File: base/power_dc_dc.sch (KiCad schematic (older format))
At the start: 14 parts

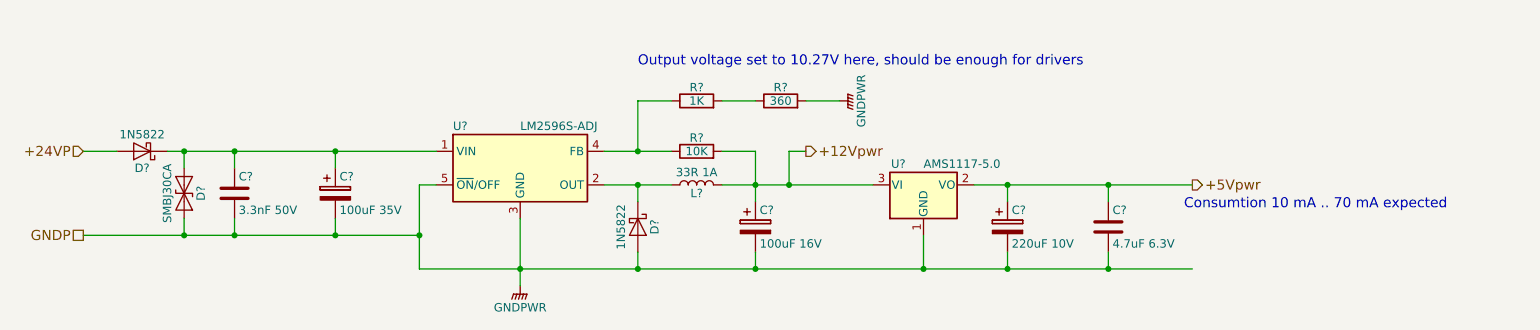
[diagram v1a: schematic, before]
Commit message: Update base board: 1. Add extra analog voltage input to core board.   -> update pinmux 2. Assign most footprints. 3. Generate netlist. 4. Add core_sf board. 5. Add kicad_symbols library submodule.
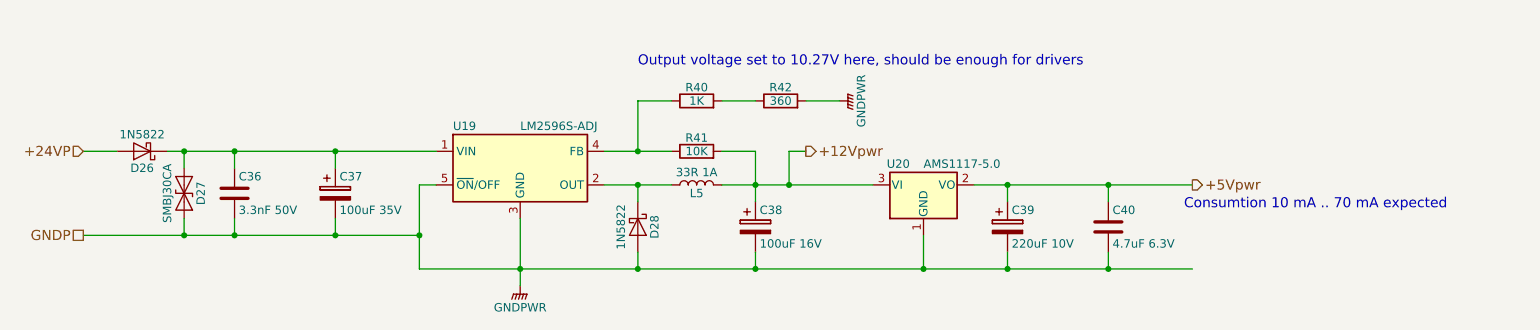
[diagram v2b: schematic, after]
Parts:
- U19: renamed from U?; footprint TO_SOT_Packages_SMD:TO-263-5_TabPin3 -> Package_TO_SOT_SMD:TO-263-5_TabPin3
- gave numbers to parts that had none: 13
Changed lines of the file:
@@
 GNDP
 $Comp
-L CP C?
+L CP C37
 U 1 1 5A3CC87A
 P 4400 1950
-F 0 "C?" H 4425 2050 50  0000 L CNN
+F 0 "C37" H 4425 2050 50  0000 L CNN
 F 1 "100uF 35V" H 4425 1850 50  0000 L CNN
 F 2 "Capacitor_SMD:CP_Elec_6.3x7.7" H 4438 1800 50  0001 C CNN
@@
 $EndComp
 $Comp
-L 1N5822 D?
+L 1N5822 D26
 U 1 1 5A3CCF01
 P 3250 1700
-F 0 "D?" H 3250 1800 50  0000 C CNN
+F 0 "D26" H 3250 1800 50  0000 C CNN
 F 1 "1N5822" H 3250 1600 50  0000 C CNN
 F 2 "Diode_SMD:D_SMA" H 3250 1525 50  0001 C CNN
@@
 $EndComp
 $Comp
-L D_TVS D?
+L D_TVS D27
 U 1 1 5A3CCF8D
 P 3500 1950
-F 0 "D?" H 3500 2050 50  0000 C CNN
+F 0 "D27" H 3500 2050 50  0000 C CNN
 F 1 "SMBJ30CA" H 3500 1850 50  0000 C CNN
 F 2 "Diode_SMD:D_SMB" H 3500 1950 50  0001 C CNN
@@
 $EndComp
 $Comp
-L C C?
+L C C36
 U 1 1 5A3CD01A
 P 3800 1950
-F 0 "C?" H 3825 2050 50  0000 L CNN
+F 0 "C36" H 3825 2050 50  0000 L CNN
 F 1 "3.3nF 50V" H 3825 1850 50  0000 L CNN
 F 2 "Capacitor_SMD:C_0603_1608Metric" H 3838 1800 50  0001 C CNN
@@
 Connection ~ 4400 1700
 $Comp
-L CP C?
+L CP C38
 U 1 1 5A3CE026
 P 6900 2150
-F 0 "C?" H 6925 2250 50  0000 L CNN
+F 0 "C38" H 6925 2250 50  0000 L CNN
 F 1 "100uF 16V" H 6925 2050 50  0000 L CNN
 F 2 "Capacitor_SMD:CP_Elec_6.3x5.3" H 6938 2000 50  0001 C CNN
@@
 $EndComp
 $Comp
-L AP1117-15 U?
+L AP1117-15 U20
 U 1 1 5A3CE6FE
 P 7900 1900
-F 0 "U?" H 7750 2025 50  0000 C CNN
+F 0 "U20" H 7750 2025 50  0000 C CNN
 F 1 "AMS1117-5.0" H 7900 2025 50  0000 L CNN
 F 2 "Package_TO_SOT_SMD:SOT-223" H 7900 2100 50  0001 C CNN
@@
 	7900 2400 7900 2200
 $Comp
-L CP C?
+L CP C39
 U 1 1 5A3CEB23
 P 8400 2150
-F 0 "C?" H 8425 2250 50  0000 L CNN
+F 0 "C39" H 8425 2250 50  0000 L CNN
 F 1 "220uF 10V" H 8425 2050 50  0000 L CNN
 F 2 "Capacitor_SMD:CP_Elec_6.3x5.3" H 8438 2000 50  0001 C CNN
@@
 	8400 1900 8400 2000
 $Comp
-L C C?
+L C C40
 U 1 1 5A3CEF52
 P 9000 2150
-F 0 "C?" H 9025 2250 50  0000 L CNN
+F 0 "C40" H 9025 2250 50  0000 L CNN
 F 1 "4.7uF 6.3V" H 9025 2050 50  0000 L CNN
 F 2 "Capacitor_SMD:C_0603_1608Metric" H 9038 2000 50  0001 C CNN
@@
 	2900 2200 4900 2200
 $Comp
-L LM2596S-ADJ U?
+L LM2596S-ADJ U19
 U 1 1 5A3D049F
 P 5500 1800
-F 0 "U?" H 5100 2050 50  0000 L CNN
+F 0 "U19" H 5100 2050 50  0000 L CNN
 F 1 "LM2596S-ADJ" H 5500 2050 50  0000 L CNN
-F 2 "TO_SOT_Packages_SMD:TO-263-5_TabPin3" H 5550 1550 50  0001 L CIN
+F 2 "Package_TO_SOT_SMD:TO-263-5_TabPin3" H 5550 1550 50  0001 L CIN
 F 3 "" H 5500 1800 50  0001 C CNN
 	1    5500 1800
@@
 $EndComp
 $Comp
-L 1N5822 D?
+L 1N5822 D28
 U 1 1 5A3D0B74
 P 6200 2150
-F 0 "D?" H 6200 2250 50  0000 C CNN
+F 0 "D28" H 6200 2250 50  0000 C CNN
 F 1 "1N5822" H 6200 2050 50  0000 C CNN
 F 2 "Diode_SMD:D_SMA" H 6200 1975 50  0001 C CNN
@@
 	6000 1900 6400 1900
 $Comp
-L L L?
+L L L5
 U 1 1 5A3D14CE
 P 6550 1900
-F 0 "L?" V 6500 1900 50  0000 C CNN
+F 0 "L5" V 6500 1900 50  0000 C CNN
 F 1 "33R 1A" V 6625 1900 50  0000 C CNN
 F 2 "Inductor_SMD:L_7.3x7.3_H3.5" H 6550 1900 50  0001 C CNN
@@
 	6000 1700 6400 1700
 $Comp
-L R R?
+L R R41
 U 1 1 5A3D2233
 P 6550 1700
-F 0 "R?" V 6630 1700 50  0000 C CNN
+F 0 "R41" V 6630 1700 50  0000 C CNN
 F 1 "10K" V 6550 1700 50  0000 C CNN
 F 2 "Resistor_SMD:R_0603_1608Metric" V 6480 1700 50  0001 C CNN
@@
 $EndComp
 $Comp
-L R R?
+L R R40
 U 1 1 5A3D2341
 P 6550 1400
-F 0 "R?" V 6630 1400 50  0000 C CNN
+F 0 "R40" V 6630 1400 50  0000 C CNN
 F 1 "1K" V 6550 1400 50  0000 C CNN
 F 2 "Resistor_SMD:R_0603_1608Metric" V 6480 1400 50  0001 C CNN
@@
 	6700 1400 6900 1400
 $Comp
-L R R?
+L R R42
 U 1 1 5A3D26F4
 P 7050 1400
-F 0 "R?" V 7130 1400 50  0000 C CNN
+F 0 "R42" V 7130 1400 50  0000 C CNN
 F 1 "360" V 7050 1400 50  0000 C CNN
 F 2 "Resistor_SMD:R_0603_1608Metric" V 6980 1400 50  0001 C CNN
@@
 	7200 1400 7400 1400
 $Comp
-L GNDPWR #PWR?
+L GNDPWR #PWR025
 U 1 1 5A3D27D8
 P 7400 1400
-F 0 "#PWR?" H 7400 1200 50  0001 C CNN
+F 0 "#PWR025" H 7400 1200 50  0001 C CNN
 F 1 "GNDPWR" H 7400 1270 50  0000 C CNN
 F 2 "" H 7400 1350 50  0001 C CNN
@@
 $EndComp
 $Comp
-L GNDPWR #PWR?
+L GNDPWR #PWR026
 U 1 1 5A3D2843
 P 5500 2500
-F 0 "#PWR?" H 5500 2300 50  0001 C CNN
+F 0 "#PWR026" H 5500 2300 50  0001 C CNN
 F 1 "GNDPWR" H 5500 2370 50  0000 C CNN
 F 2 "" H 5500 2450 50  0001 C CNN

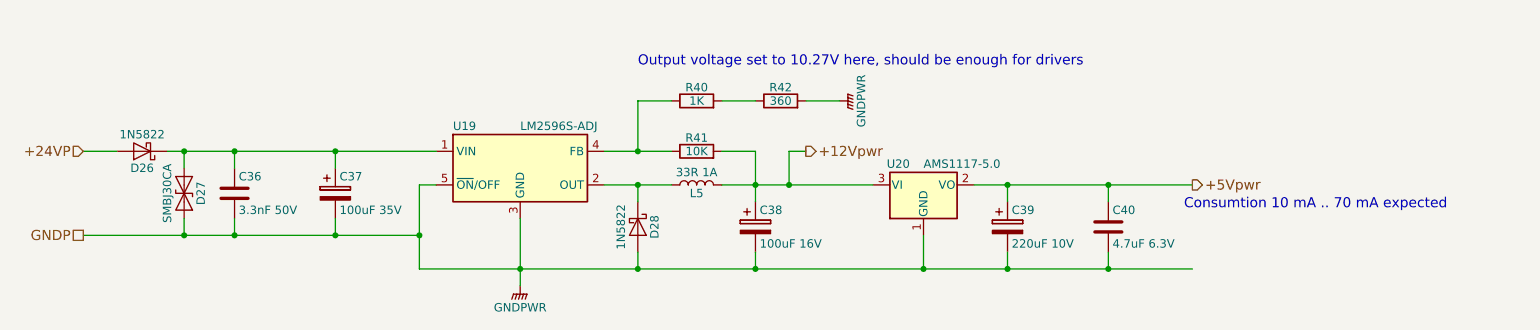
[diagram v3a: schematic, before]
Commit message: some test points
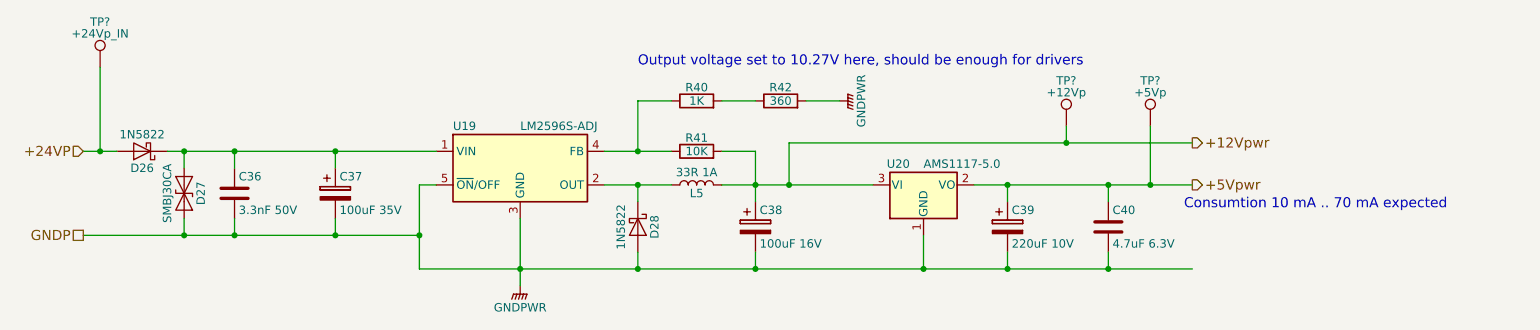
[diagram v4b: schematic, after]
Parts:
- added TP?: +24Vp_IN, symbol Test_Point
- added TP?: +12Vp, symbol Test_Point
- added TP?: +5Vp, symbol Test_Point
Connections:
- net +12Vpwr: now also TP?.1
- net +24VP: now also TP?.1
- net +5Vpwr: now also TP?.1
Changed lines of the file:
@@
 Text HLabel 2900 1700 0    60   Input ~ 0
 +24VP
-Text HLabel 7200 1700 2    60   Output ~ 0
+Text HLabel 9500 1650 2    60   Output ~ 0
 +12Vpwr
 Text HLabel 9500 1900 2    60   Output ~ 0
@@
 	1    0    0    -1
 $EndComp
-Wire Wire Line
-	3400 1700 5000 1700
-Wire Wire Line
-	2900 1700 3100 1700
-Wire Wire Line
-	3500 1800 3500 1700
-Connection ~ 3500 1700
-Wire Wire Line
-	4400 2100 4400 2200
-Connection ~ 4400 2200
-Wire Wire Line
-	3800 2100 3800 2200
-Connection ~ 3800 2200
-Wire Wire Line
-	3500 2100 3500 2200
-Connection ~ 3500 2200
-Wire Wire Line
-	3800 1800 3800 1700
-Connection ~ 3800 1700
-Wire Wire Line
-	4400 1800 4400 1700
-Connection ~ 4400 1700
 $Comp
 L CP C38
@@
 	1    0    0    -1
 $EndComp
-Wire Wire Line
-	7900 2400 7900 2200
 $Comp
 L CP C39
@@
 	1    0    0    -1
 $EndComp
-Wire Wire Line
-	8200 1900 9500 1900
-Wire Wire Line
-	8400 1900 8400 2000
 $Comp
 L C C40
@@
 	1    0    0    -1
 $EndComp
-Connection ~ 8400 1900
-Wire Wire Line
-	9000 2000 9000 1900
-Connection ~ 9000 1900
-Wire Wire Line
-	2900 2200 4900 2200
 $Comp
 L LM2596S-ADJ U19
@@
 	0    1    1    0
 $EndComp
-Wire Wire Line
-	4900 1900 4900 2400
-Wire Wire Line
-	4900 1900 5000 1900
-Wire Wire Line
-	4900 2400 9500 2400
-Connection ~ 4900 2200
-Wire Wire Line
-	5500 2100 5500 2500
-Connection ~ 5500 2400
-Wire Wire Line
-	6200 2400 6200 2300
-Connection ~ 6200 2400
-Wire Wire Line
-	6200 2000 6200 1900
-Wire Wire Line
-	6000 1900 6400 1900
 $Comp
 L L L5
@@
 	0    -1   -1   0
 $EndComp
-Connection ~ 6200 1900
-Wire Wire Line
-	6000 1700 6400 1700
 $Comp
 L R R41
@@
 	0    -1   -1   0
 $EndComp
-Wire Wire Line
-	6200 1700 6200 1400
-Wire Wire Line
-	6200 1400 6400 1400
-Connection ~ 6200 1700
-Wire Wire Line
-	6700 1400 6900 1400
 $Comp
 L R R42
@@
 	0    -1   -1   0
 $EndComp
-Wire Wire Line
-	7200 1400 7400 1400
 $Comp
 L GNDPWR #PWR025
@@
 	1    0    0    -1
 $EndComp
-Wire Wire Line
-	6700 1700 6900 1700
-Wire Wire Line
-	6900 1700 6900 2000
-Wire Wire Line
-	6700 1900 7600 1900
-Connection ~ 6900 1900
-Wire Wire Line
-	6900 2400 6900 2300
-Connection ~ 6900 2400
-Wire Wire Line
-	7100 1900 7100 1700
-Wire Wire Line
-	7100 1700 7200 1700
-Connection ~ 7100 1900
-Wire Wire Line
-	8400 2400 8400 2300
-Connection ~ 7900 2400
-Wire Wire Line
-	9000 2400 9000 2300
-Connection ~ 8400 2400
-Connection ~ 9000 2400
 Text Notes 6200 1200 0    60   ~ 0
 Output voltage set to 10.27V here, should be enough for drivers
 Text Notes 9450 2050 0    60   ~ 0
 Consumtion 10 mA .. 70 mA expected
+$Comp
+L Test_Point TP?
+U 1 1 5A4A3905
+P 3000 1200
+F 0 "TP?" H 3000 1470 50  0000 C CNN
+F 1 "+24Vp_IN" H 3000 1400 50  0000 C CNN
+F 2 "" H 3200 1200 50  0001 C CNN
+F 3 "" H 3200 1200 50  0001 C CNN
+	1    3000 1200
+	1    0    0    -1
+$EndComp
+$Comp
+L Test_Point TP?
+U 1 1 5A4A3B60
+P 8750 1550
+F 0 "TP?" H 8750 1820 50  0000 C CNN
+F 1 "+12Vp" H 8750 1750 50  0000 C CNN
+F 2 "" H 8950 1550 50  0001 C CNN
+F 3 "" H 8950 1550 50  0001 C CNN
+	1    8750 1550
+	1    0    0    -1
+$EndComp
+$Comp
+L Test_Point TP?
+U 1 1 5A4A3BA9
+P 9250 1550
+F 0 "TP?" H 9250 1820 50  0000 C CNN
+F 1 "+5Vp" H 9250 1750 50  0000 C CNN
+F 2 "" H 9450 1550 50  0001 C CNN
+F 3 "" H 9450 1550 50  0001 C CNN
+	1    9250 1550
+	1    0    0    -1
+$EndComp
+Connection ~ 9250 1900
+Wire Wire Line
+	9250 1550 9250 1900
+Connection ~ 8750 1650
+Wire Wire Line
+	8750 1550 8750 1650
+Connection ~ 3000 1700
+Wire Wire Line
+	3000 1200 3000 1700
+Connection ~ 9000 2400
+Connection ~ 8400 2400
+Wire Wire Line
+	9000 2400 9000 2300
+Connection ~ 7900 2400
+Wire Wire Line
+	8400 2400 8400 2300
+Connection ~ 7100 1900
+Wire Wire Line
+	7100 1650 9500 1650
+Wire Wire Line
+	7100 1900 7100 1650
+Connection ~ 6900 2400
+Wire Wire Line
+	6900 2400 6900 2300
+Connection ~ 6900 1900
+Wire Wire Line
+	6700 1900 7600 1900
+Wire Wire Line
+	6900 1700 6900 2000
+Wire Wire Line
+	6700 1700 6900 1700
+Wire Wire Line
+	7200 1400 7400 1400
+Wire Wire Line
+	6700 1400 6900 1400
+Connection ~ 6200 1700
+Wire Wire Line
+	6200 1400 6400 1400
+Wire Wire Line
+	6200 1700 6200 1400
+Wire Wire Line
+	6000 1700 6400 1700
+Connection ~ 6200 1900
+Wire Wire Line
+	6000 1900 6400 1900
+Wire Wire Line
+	6200 2000 6200 1900
+Connection ~ 6200 2400
+Wire Wire Line
+	6200 2400 6200 2300
+Connection ~ 5500 2400
+Wire Wire Line
+	5500 2100 5500 2500
+Connection ~ 4900 2200
+Wire Wire Line
+	4900 2400 9500 2400
+Wire Wire Line
+	4900 1900 5000 1900
+Wire Wire Line
+	4900 1900 4900 2400
+Wire Wire Line
+	2900 2200 4900 2200
+Connection ~ 9000 1900
+Wire Wire Line
+	9000 2000 9000 1900
+Connection ~ 8400 1900
+Wire Wire Line
+	8400 1900 8400 2000
+Wire Wire Line
+	8200 1900 9500 1900
+Wire Wire Line
+	7900 2400 7900 2200
+Connection ~ 4400 1700
+Wire Wire Line
+	4400 1800 4400 1700
+Connection ~ 3800 1700
+Wire Wire Line
+	3800 1800 3800 1700
+Connection ~ 3500 2200
+Wire Wire Line
+	3500 2100 3500 2200
+Connection ~ 3800 2200
+Wire Wire Line
+	3800 2200 3800 2100
+Connection ~ 4400 2200
+Wire Wire Line
+	4400 2200 4400 2100
+Connection ~ 3500 1700
+Wire Wire Line
+	3500 1800 3500 1700
+Wire Wire Line
+	2900 1700 3100 1700
+Wire Wire Line
+	3400 1700 5000 1700
 $EndSCHEMATC

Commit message: annotate sch
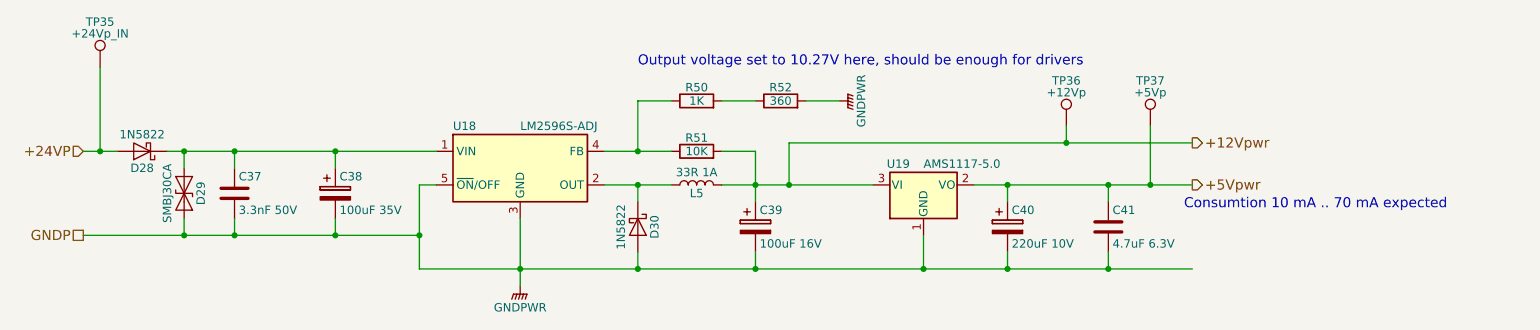
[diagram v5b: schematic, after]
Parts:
- gave numbers to parts that had none: 3
- renumbered C36 to C37, C37 to C38, C38 to C39, C39 to C40, C40 to C41, D26 to D28, D27 to D29, D28 to D30, R40 to R50, R41 to R51, R42 to R52, U19 to U18, U20 to U19
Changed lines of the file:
@@
 GNDP
 $Comp
-L CP C37
+L CP C38
 U 1 1 5A3CC87A
 P 4400 1950
-F 0 "C37" H 4425 2050 50  0000 L CNN
+F 0 "C38" H 4425 2050 50  0000 L CNN
 F 1 "100uF 35V" H 4425 1850 50  0000 L CNN
 F 2 "Capacitor_SMD:CP_Elec_6.3x7.7" H 4438 1800 50  0001 C CNN
@@
 $EndComp
 $Comp
-L 1N5822 D26
+L 1N5822 D28
 U 1 1 5A3CCF01
 P 3250 1700
-F 0 "D26" H 3250 1800 50  0000 C CNN
+F 0 "D28" H 3250 1800 50  0000 C CNN
 F 1 "1N5822" H 3250 1600 50  0000 C CNN
 F 2 "Diode_SMD:D_SMA" H 3250 1525 50  0001 C CNN
@@
 $EndComp
 $Comp
-L D_TVS D27
+L D_TVS D29
 U 1 1 5A3CCF8D
 P 3500 1950
-F 0 "D27" H 3500 2050 50  0000 C CNN
+F 0 "D29" H 3500 2050 50  0000 C CNN
 F 1 "SMBJ30CA" H 3500 1850 50  0000 C CNN
 F 2 "Diode_SMD:D_SMB" H 3500 1950 50  0001 C CNN
@@
 $EndComp
 $Comp
-L C C36
+L C C37
 U 1 1 5A3CD01A
 P 3800 1950
-F 0 "C36" H 3825 2050 50  0000 L CNN
+F 0 "C37" H 3825 2050 50  0000 L CNN
 F 1 "3.3nF 50V" H 3825 1850 50  0000 L CNN
 F 2 "Capacitor_SMD:C_0603_1608Metric" H 3838 1800 50  0001 C CNN
@@
 $EndComp
 $Comp
-L CP C38
+L CP C39
 U 1 1 5A3CE026
 P 6900 2150
-F 0 "C38" H 6925 2250 50  0000 L CNN
+F 0 "C39" H 6925 2250 50  0000 L CNN
 F 1 "100uF 16V" H 6925 2050 50  0000 L CNN
 F 2 "Capacitor_SMD:CP_Elec_6.3x5.3" H 6938 2000 50  0001 C CNN
@@
 $EndComp
 $Comp
-L AP1117-15 U20
+L AP1117-15 U19
 U 1 1 5A3CE6FE
 P 7900 1900
-F 0 "U20" H 7750 2025 50  0000 C CNN
+F 0 "U19" H 7750 2025 50  0000 C CNN
 F 1 "AMS1117-5.0" H 7900 2025 50  0000 L CNN
 F 2 "Package_TO_SOT_SMD:SOT-223" H 7900 2100 50  0001 C CNN
@@
 $EndComp
 $Comp
-L CP C39
+L CP C40
 U 1 1 5A3CEB23
 P 8400 2150
-F 0 "C39" H 8425 2250 50  0000 L CNN
+F 0 "C40" H 8425 2250 50  0000 L CNN
 F 1 "220uF 10V" H 8425 2050 50  0000 L CNN
 F 2 "Capacitor_SMD:CP_Elec_6.3x5.3" H 8438 2000 50  0001 C CNN
@@
 $EndComp
 $Comp
-L C C40
+L C C41
 U 1 1 5A3CEF52
 P 9000 2150
-F 0 "C40" H 9025 2250 50  0000 L CNN
+F 0 "C41" H 9025 2250 50  0000 L CNN
 F 1 "4.7uF 6.3V" H 9025 2050 50  0000 L CNN
 F 2 "Capacitor_SMD:C_0603_1608Metric" H 9038 2000 50  0001 C CNN
@@
 $EndComp
 $Comp
-L LM2596S-ADJ U19
+L LM2596S-ADJ U18
 U 1 1 5A3D049F
 P 5500 1800
-F 0 "U19" H 5100 2050 50  0000 L CNN
+F 0 "U18" H 5100 2050 50  0000 L CNN
 F 1 "LM2596S-ADJ" H 5500 2050 50  0000 L CNN
 F 2 "Package_TO_SOT_SMD:TO-263-5_TabPin3" H 5550 1550 50  0001 L CIN
@@
 $EndComp
 $Comp
-L 1N5822 D28
+L 1N5822 D30
 U 1 1 5A3D0B74
 P 6200 2150
-F 0 "D28" H 6200 2250 50  0000 C CNN
+F 0 "D30" H 6200 2250 50  0000 C CNN
 F 1 "1N5822" H 6200 2050 50  0000 C CNN
 F 2 "Diode_SMD:D_SMA" H 6200 1975 50  0001 C CNN
@@
 $EndComp
 $Comp
-L R R41
+L R R51
 U 1 1 5A3D2233
 P 6550 1700
-F 0 "R41" V 6630 1700 50  0000 C CNN
+F 0 "R51" V 6630 1700 50  0000 C CNN
 F 1 "10K" V 6550 1700 50  0000 C CNN
 F 2 "Resistor_SMD:R_0603_1608Metric" V 6480 1700 50  0001 C CNN
@@
 $EndComp
 $Comp
-L R R40
+L R R50
 U 1 1 5A3D2341
 P 6550 1400
-F 0 "R40" V 6630 1400 50  0000 C CNN
+F 0 "R50" V 6630 1400 50  0000 C CNN
 F 1 "1K" V 6550 1400 50  0000 C CNN
 F 2 "Resistor_SMD:R_0603_1608Metric" V 6480 1400 50  0001 C CNN
@@
 $EndComp
 $Comp
-L R R42
+L R R52
 U 1 1 5A3D26F4
 P 7050 1400
-F 0 "R42" V 7130 1400 50  0000 C CNN
+F 0 "R52" V 7130 1400 50  0000 C CNN
 F 1 "360" V 7050 1400 50  0000 C CNN
 F 2 "Resistor_SMD:R_0603_1608Metric" V 6980 1400 50  0001 C CNN
@@
 $EndComp
 $Comp
-L GNDPWR #PWR025
+L GNDPWR #PWR32
 U 1 1 5A3D27D8
 P 7400 1400
-F 0 "#PWR025" H 7400 1200 50  0001 C CNN
+F 0 "#PWR32" H 7400 1200 50  0001 C CNN
 F 1 "GNDPWR" H 7400 1270 50  0000 C CNN
 F 2 "" H 7400 1350 50  0001 C CNN
@@
 $EndComp
 $Comp
-L GNDPWR #PWR026
+L GNDPWR #PWR31
 U 1 1 5A3D2843
 P 5500 2500
-F 0 "#PWR026" H 5500 2300 50  0001 C CNN
+F 0 "#PWR31" H 5500 2300 50  0001 C CNN
 F 1 "GNDPWR" H 5500 2370 50  0000 C CNN
 F 2 "" H 5500 2450 50  0001 C CNN
@@
 Consumtion 10 mA .. 70 mA expected
 $Comp
-L Test_Point TP?
+L Test_Point TP35
 U 1 1 5A4A3905
 P 3000 1200
-F 0 "TP?" H 3000 1470 50  0000 C CNN
+F 0 "TP35" H 3000 1470 50  0000 C CNN
 F 1 "+24Vp_IN" H 3000 1400 50  0000 C CNN
 F 2 "" H 3200 1200 50  0001 C CNN
@@
 $EndComp
 $Comp
-L Test_Point TP?
+L Test_Point TP36
 U 1 1 5A4A3B60
 P 8750 1550
-F 0 "TP?" H 8750 1820 50  0000 C CNN
+F 0 "TP36" H 8750 1820 50  0000 C CNN
 F 1 "+12Vp" H 8750 1750 50  0000 C CNN
 F 2 "" H 8950 1550 50  0001 C CNN
@@
 $EndComp
 $Comp
-L Test_Point TP?
+L Test_Point TP37
 U 1 1 5A4A3BA9
 P 9250 1550
-F 0 "TP?" H 9250 1820 50  0000 C CNN
+F 0 "TP37" H 9250 1820 50  0000 C CNN
 F 1 "+5Vp" H 9250 1750 50  0000 C CNN
 F 2 "" H 9450 1550 50  0001 C CNN

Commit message: added footprints, created netlist
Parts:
- TP35, TP36, TP37: footprint (none) -> TestPoint:TestPoint_Pad_D1.5mm
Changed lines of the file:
@@
 $EndComp
 $Comp
-L GNDPWR #PWR32
+L GNDPWR #PWR031
 U 1 1 5A3D27D8
 P 7400 1400
-F 0 "#PWR32" H 7400 1200 50  0001 C CNN
+F 0 "#PWR031" H 7400 1200 50  0001 C CNN
 F 1 "GNDPWR" H 7400 1270 50  0000 C CNN
 F 2 "" H 7400 1350 50  0001 C CNN
@@
 $EndComp
 $Comp
-L GNDPWR #PWR31
+L GNDPWR #PWR032
 U 1 1 5A3D2843
 P 5500 2500
-F 0 "#PWR31" H 5500 2300 50  0001 C CNN
+F 0 "#PWR032" H 5500 2300 50  0001 C CNN
 F 1 "GNDPWR" H 5500 2370 50  0000 C CNN
 F 2 "" H 5500 2450 50  0001 C CNN
@@
 F 0 "TP35" H 3000 1470 50  0000 C CNN
 F 1 "+24Vp_IN" H 3000 1400 50  0000 C CNN
-F 2 "" H 3200 1200 50  0001 C CNN
+F 2 "TestPoint:TestPoint_Pad_D1.5mm" H 3200 1200 50  0001 C CNN
 F 3 "" H 3200 1200 50  0001 C CNN
 	1    3000 1200
@@
 F 0 "TP36" H 8750 1820 50  0000 C CNN
 F 1 "+12Vp" H 8750 1750 50  0000 C CNN
-F 2 "" H 8950 1550 50  0001 C CNN
+F 2 "TestPoint:TestPoint_Pad_D1.5mm" H 8950 1550 50  0001 C CNN
 F 3 "" H 8950 1550 50  0001 C CNN
 	1    8750 1550
@@
 F 0 "TP37" H 9250 1820 50  0000 C CNN
 F 1 "+5Vp" H 9250 1750 50  0000 C CNN
-F 2 "" H 9450 1550 50  0001 C CNN
+F 2 "TestPoint:TestPoint_Pad_D1.5mm" H 9450 1550 50  0001 C CNN
 F 3 "" H 9450 1550 50  0001 C CNN
 	1    9250 1550

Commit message: upd
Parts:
- renumbered C37 to C35, C38 to C36, C39 to C37, C40 to C38, C41 to C39
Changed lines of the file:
@@
 GNDP
 $Comp
-L CP C38
+L CP C36
 U 1 1 5A3CC87A
 P 4400 1950
-F 0 "C38" H 4425 2050 50  0000 L CNN
+F 0 "C36" H 4425 2050 50  0000 L CNN
 F 1 "100uF 35V" H 4425 1850 50  0000 L CNN
 F 2 "Capacitor_SMD:CP_Elec_6.3x7.7" H 4438 1800 50  0001 C CNN
@@
 $EndComp
 $Comp
-L C C37
+L C C35
 U 1 1 5A3CD01A
 P 3800 1950
-F 0 "C37" H 3825 2050 50  0000 L CNN
+F 0 "C35" H 3825 2050 50  0000 L CNN
 F 1 "3.3nF 50V" H 3825 1850 50  0000 L CNN
 F 2 "Capacitor_SMD:C_0603_1608Metric" H 3838 1800 50  0001 C CNN
@@
 $EndComp
 $Comp
-L CP C39
+L CP C37
 U 1 1 5A3CE026
 P 6900 2150
-F 0 "C39" H 6925 2250 50  0000 L CNN
+F 0 "C37" H 6925 2250 50  0000 L CNN
 F 1 "100uF 16V" H 6925 2050 50  0000 L CNN
 F 2 "Capacitor_SMD:CP_Elec_6.3x5.3" H 6938 2000 50  0001 C CNN
@@
 $EndComp
 $Comp
-L CP C40
+L CP C38
 U 1 1 5A3CEB23
 P 8400 2150
-F 0 "C40" H 8425 2250 50  0000 L CNN
+F 0 "C38" H 8425 2250 50  0000 L CNN
 F 1 "220uF 10V" H 8425 2050 50  0000 L CNN
 F 2 "Capacitor_SMD:CP_Elec_6.3x5.3" H 8438 2000 50  0001 C CNN
@@
 $EndComp
 $Comp
-L C C41
+L C C39
 U 1 1 5A3CEF52
 P 9000 2150
-F 0 "C41" H 9025 2250 50  0000 L CNN
+F 0 "C39" H 9025 2250 50  0000 L CNN
 F 1 "4.7uF 6.3V" H 9025 2050 50  0000 L CNN
 F 2 "Capacitor_SMD:C_0603_1608Metric" H 9038 2000 50  0001 C CNN
